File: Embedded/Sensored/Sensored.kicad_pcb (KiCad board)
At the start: 2 copper layers, 9 x 9.5 mm, 13 parts, among them U1 ICM-20948, U3 BME280

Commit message: Added Castellated Pins & Removed Micro SD Card
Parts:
- removed C10: 22uF, Capacitor_SMD:C_0603_1608Metric_Pad1.08x0.95mm_HandSolder
- removed C12: 0.1uF, Capacitor_SMD:C_0402_1005Metric
- added J1: Casselation, Simple_Connector:1mm_4P, F.Cu at (146.0, 109.5)
- added R1: 10K, Resistor_SMD:R_0402_1005Metric, F.Cu at (143.7, 105.5)
- added R2: 10K, Resistor_SMD:R_0402_1005Metric, F.Cu at (143.7, 104.6)
- moved C9 0.94 mm to (140.2, 111.3)
- moved C3 0.84 mm to (144.5, 111.2)
- moved C4 0.72 mm to (142.7, 111.3)
- moved U4 0.70 mm to (140.1, 109.9)
- moved C11 0.63 mm to (139.8, 108.5)
- moved C13 0.39 mm to (139.8, 107.3)
- moved C1 0.37 mm to (143.7, 106.5)
- moved C6 0.23 mm to (138.7, 105.9)
- moved C8 0.19 mm to (142.4, 106.0)
- moved U3 0.13 mm to (140.5, 105.5)
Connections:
- C9 pad 1: Vin -> +3V3
- U4 pad 3: Vin -> +3V3
- U4 pad 4: Vin -> +3V3
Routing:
- added copper zone on F.Cu, net +3V3
- added copper zone on B.Cu, net GND
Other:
- board size 9 x 9.5 mm -> 8 x 7.9 mm

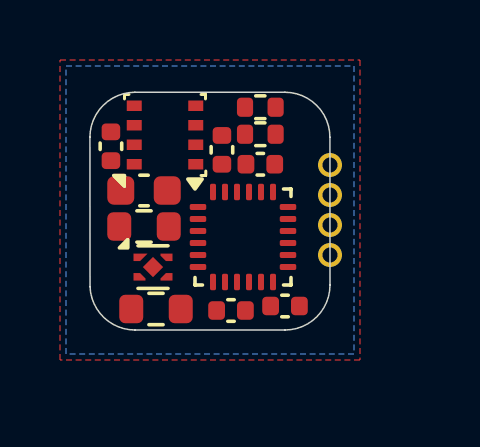
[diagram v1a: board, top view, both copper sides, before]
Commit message: Added Stabiliser GND Pins & Finished Routing
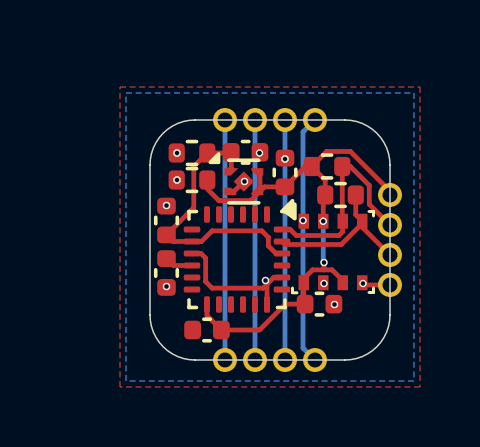
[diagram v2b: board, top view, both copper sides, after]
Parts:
- added J2: Casselation, Simple_Connector:1mm_4P, F.Cu at (142.5, 105.0)
- added J3: Casselation, Simple_Connector:1mm_4P, F.Cu at (142.5, 113.0)
- C11, C9: footprint Resistor_SMD:R_0603_1608Metric -> Resistor_SMD:R_0402_1005Metric
- C13: footprint Capacitor_SMD:C_0603_1608Metric -> Capacitor_SMD:C_0402_1005Metric
- moved U3 6.82 mm to (146.1, 109.4), turned to 0 degrees
- moved C8 6.08 mm to (145.7, 111.1), turned to 0 degrees
- moved C6 5.87 mm to (144.5, 106.8), turned to -90 degrees
- moved C9 4.46 mm to (141.4, 107.0)
- moved U4 4.16 mm to (143.1, 107.1)
- moved C1 3.65 mm to (140.6, 108.3), turned to -90 degrees
- moved C13 3.62 mm to (143.2, 106.1), turned to 0 degrees
- moved R1 3.35 mm to (146.3, 107.5)
- moved R2 2.97 mm to (145.9, 106.5)
- moved C11 2.93 mm to (141.4, 106.1)
- moved J1 2.83 mm to (148.0, 107.5), turned to 0 degrees
- moved C3 2.72 mm to (141.9, 112.0)
- moved C4 2.49 mm to (140.5, 110.1), turned to -90 degrees
- moved U1 0.78 mm to (142.9, 109.6), turned to -90 degrees
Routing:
- net GND: track 0.00 -> 39.1 mm, vias 0 -> 12
- net +3V3: track 0.00 -> 18.7 mm, vias 0 -> 2
- net +1V8: track 0.00 -> 9.37 mm
- net SDA: track 0.00 -> 7.11 mm
- net SCL: track 0.00 -> 5.66 mm
- net Net-(U1-REGOUT): track 0.00 -> 0.95 mm
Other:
- board size 8 x 7.9 mm -> 8 x 8 mm

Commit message: Added Markings & Component Adjustment
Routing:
- net GND: vias 12 -> 13
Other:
- board text added: "3V3 SDA SCL GND"

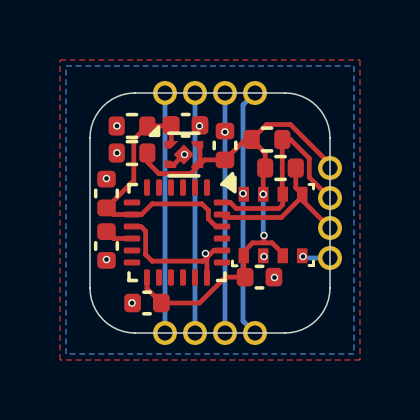
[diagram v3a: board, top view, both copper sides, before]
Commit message: Replaced Side GND Pins with GND EPad
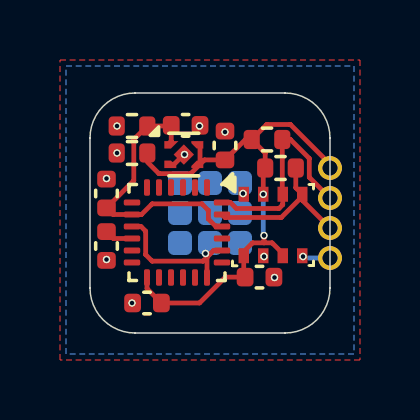
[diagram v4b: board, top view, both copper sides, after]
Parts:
- removed J3: Casselation, Simple_Connector:1mm_4P
- J2: value Casselation -> EPad; footprint Simple_Connector:1mm_4P -> Simple_Connector:1mm 3x3 Pad; moved to B.Cu
- moved J2 4.27 mm to (144.0, 109.0)
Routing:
- net GND: track 39.1 -> 6.80 mm

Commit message: Generated BOM, JLCPCB Assembly Parts, Production Files, Drill Positions
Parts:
- U4: value ~ -> TLV74018PDQNR
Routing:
- net (no net): vias 0 -> 4
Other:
- board size 8 x 8 mm -> 15 x 15 mm
- board text added: "Sensored"
- board text added: "V1.0"

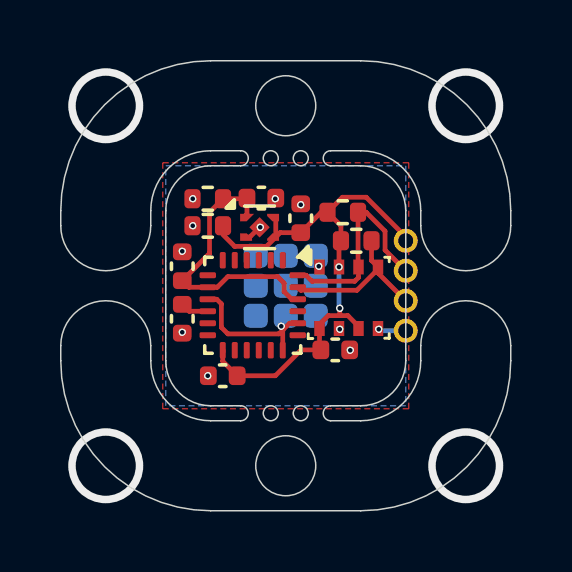
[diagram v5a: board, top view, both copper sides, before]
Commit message: Optimised JLCPCB Specific Parts
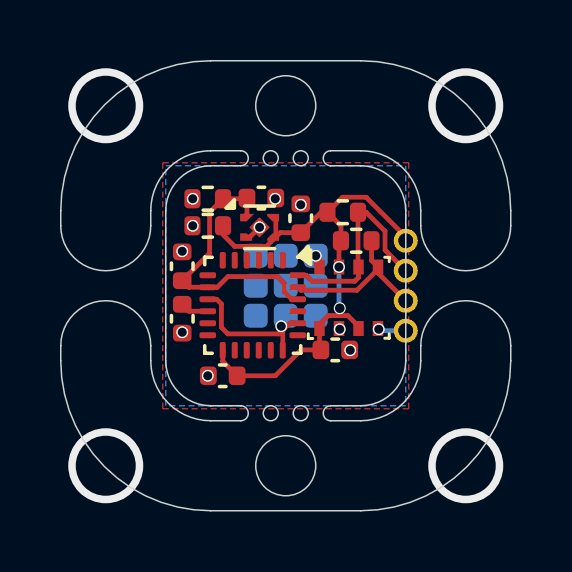
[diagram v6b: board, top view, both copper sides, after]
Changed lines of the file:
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@@
-	)
-	(segment
-		(start 145.124999 108.375)
-		(end 145.124999 108.374999)
-		(width 0.16)
-		(layer "F.Cu")
-		(net 1)
 	)
 	(segment
@@
 	)
 	(segment
-		(start 143.1275 107.0525)
-		(end 143.1475 107.0525)
-		(width 0.16)
-		(layer "F.Cu")
-		(net 1)
-	)
-	(segment
 		(start 141.42 112)
 		(end 141.4 112)
@@
 	)
 	(segment
+		(start 145.124999 108.124999)
+		(end 145.124999 108.375)
+		(width 0.16)
+		(layer "F.Cu")
+		(net 1)
+	)
+	(segment
 		(start 143.9 110.4)
 		(end 143.85 110.35)
@@
 	)
 	(segment
-		(start 143.1475 107.0525)
-		(end 143.15 107.05)
-		(width 0.16)
-		(layer "F.Cu")
-		(net 1)
-	)
-	(segment
 		(start 141.4 109.449999)
 		(end 141.699999 109.449999)
@@
 	)
 	(segment
+		(start 145 108)
+		(end 145.124999 108.124999)
+		(width 0.16)
+		(layer "F.Cu")
+		(net 1)
+	)
+	(segment
 		(start 140.89 107)
 		(end 140.9 107)
@@
 	)
 	(segment
-		(start 145.124999 108.374999)
-		(end 145.1 108.35)
-		(width 0.16)
-		(layer "F.Cu")
-		(net 1)
-	)
-	(segment
 		(start 142.5875 107.3775)
 		(end 142.8025 107.3775)
@@
 	)
 	(via
-		(at 143.15 107.05)
-		(size 0.25)
-		(drill 0.15)
+		(at 143.1275 107.0525)
+		(size 0.4)
+		(drill 0.3)
 		(layers "F.Cu" "B.Cu")
 		(net 1)
@@
 	(via
 		(at 140.9 106.1)
-		(size 0.25)
-		(drill 0.15)
+		(size 0.4)
+		(drill 0.3)
 		(layers "F.Cu" "B.Cu")
 		(net 1)
@@
 	(via
 		(at 140.55 107.85)
-		(size 0.25)
-		(drill 0.15)
+		(size 0.4)
+		(drill 0.3)
 		(layers "F.Cu" "B.Cu")
 		(net 1)
@@
 	(via
 		(at 140.9 107)
-		(size 0.25)
-		(drill 0.15)
+		(size 0.4)
+		(drill 0.3)
 		(layers "F.Cu" "B.Cu")
 		(net 1)
@@
 	(via
 		(at 146.15 111.15)
-		(size 0.25)
-		(drill 0.15)
+		(size 0.4)
+		(drill 0.3)
 		(layers "F.Cu" "B.Cu")
 		(net 1)
@@
 	(via
 		(at 141.4 112)
-		(size 0.25)
-		(drill 0.15)
+		(size 0.4)
+		(drill 0.3)
 		(layers "F.Cu" "B.Cu")
 		(net 1)
@@
 	(via
 		(at 143.85 110.35)
-		(size 0.25)
-		(drill 0.15)
-		(layers "F.Cu" "B.Cu")
-		(net 1)
-	)
-	(via
-		(at 145.1 108.35)
-		(size 0.25)
-		(drill 0.15)
+		(size 0.4)
+		(drill 0.3)
+		(layers "F.Cu" "B.Cu")
+		(net 1)
+	)
+	(via
+		(at 145 108)
+		(size 0.4)
+		(drill 0.3)
 		(layers "F.Cu" "B.Cu")
 		(net 1)
@@
 	(via
 		(at 145.8 110.45)
-		(size 0.25)
-		(drill 0.15)
+		(size 0.4)
+		(drill 0.3)
 		(layers "F.Cu" "B.Cu")
 		(net 1)
@@
 	(via
 		(at 147.1 110.45)
-		(size 0.25)
-		(drill 0.15)
+		(size 0.4)
+		(drill 0.3)
 		(layers "F.Cu" "B.Cu")
 		(net 1)
@@
 	(via
 		(at 144.5 106.3)
-		(size 0.25)
-		(drill 0.15)
+		(size 0.4)
+		(drill 0.3)
 		(layers "F.Cu" "B.Cu")
 		(net 1)
@@
 	(via
 		(at 140.55 110.55)
-		(size 0.25)
-		(drill 0.15)
+		(size 0.4)
+		(drill 0.3)
 		(layers "F.Cu" "B.Cu")
 		(net 1)
@@
 	(via
 		(at 143.65 106.1)
-		(size 0.25)
-		(drill 0.15)
+		(size 0.4)
+		(drill 0.3)
 		(layers "F.Cu" "B.Cu")
 		(net 1)
@@
 	(via
 		(at 145.8 109.75)
-		(size 0.25)
-		(drill 0.15)
+		(size 0.4)
+		(drill 0.32)
 		(layers "F.Cu" "B.Cu")
 		(net 3)
@@
 	(via
 		(at 145.775 108.375)
-		(size 0.25)
-		(drill 0.15)
-		(layers "F.Cu" "B.Cu")
-		(net 3)
+		(size 0.4)
+		(drill 0.3)
+		(layers "F.Cu" "B.Cu")
+		(net 3)

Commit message: Removed Obsolete Files
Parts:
- C6, C8: value 100nF -> 0.1uF
- U4: value TLV74018PDQNR -> TLV74318PDQNR3
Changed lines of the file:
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@@
 			)
 		)
-		(property "LCSC" ""
+		(property "LCSC" "C52923"
 			(at 0 0 180)
 			(unlocked yes)
@@
 			)
 		)
-		(property "LCSC" ""
+		(property "LCSC" "C1525"
 			(at 0 0 -90)
 			(unlocked yes)
@@
 			)
 		)
-		(property "LCSC" ""
+		(property "LCSC" "C92489"
 			(at 0 0 0)
 			(unlocked yes)
@@
 			)
 		)
-		(property "LCSC" ""
+		(property "LCSC" "C1525"
 			(at 0 0 180)
 			(unlocked yes)
@@
 			)
 		)
-		(property "LCSC" ""
+		(property "LCSC" "C25744"
 			(at 0 0 0)
 			(unlocked yes)
@@
 			)
 		)
-		(property "LCSC" ""
+		(property "LCSC" "C1525"
 			(at 0 0 -90)
 			(unlocked yes)
@@
 			)
 		)
-		(property "Value" "100nF"
+		(property "Value" "0.1uF"
 			(at 0 1.16 90)
 			(layer "F.Fab")
@@
 			)
 		)
-		(property "LCSC" ""
+		(property "LCSC" "C1525"
 			(at 0 0 -90)
 			(unlocked yes)
@@
 			)
 		)
-		(property "Value" "100nF"
+		(property "Value" "0.1uF"
 			(at 0 1.16 0)
 			(layer "F.Fab")
@@
 			)
 		)
-		(property "LCSC" ""
+		(property "LCSC" "C1525"
 			(at 0 0 0)
 			(unlocked yes)
@@
 			)
 		)
-		(property "LCSC" ""
+		(property "LCSC" "C15525"
 			(at 0 0 0)
 			(unlocked yes)
@@
 			)
 		)
-		(property "LCSC" ""
+		(property "LCSC" "C25744"
 			(at 0 0 0)
 			(unlocked yes)
@@
 			)
 		)
-		(property "Value" "TLV74018PDQNR"
+		(property "Value" "TLV74318PDQNR3"
 			(at 0 1.5 0)
 			(layer "F.Fab")
@@
 			)
 		)
-		(property "LCSC" ""
+		(property "LCSC PN" "C2860843"
 			(at 0 0 0)
 			(unlocked yes)
@@
 			)
 		)
-		(property "LCSC" ""
+		(property "LCSC" "C52923"
 			(at 0 0 180)
 			(unlocked yes)
@@
 			)
 		)
-		(property "LCSC" ""
+		(property "LCSC PN" "C726001"
 			(at 0 0 -90)
 			(unlocked yes)

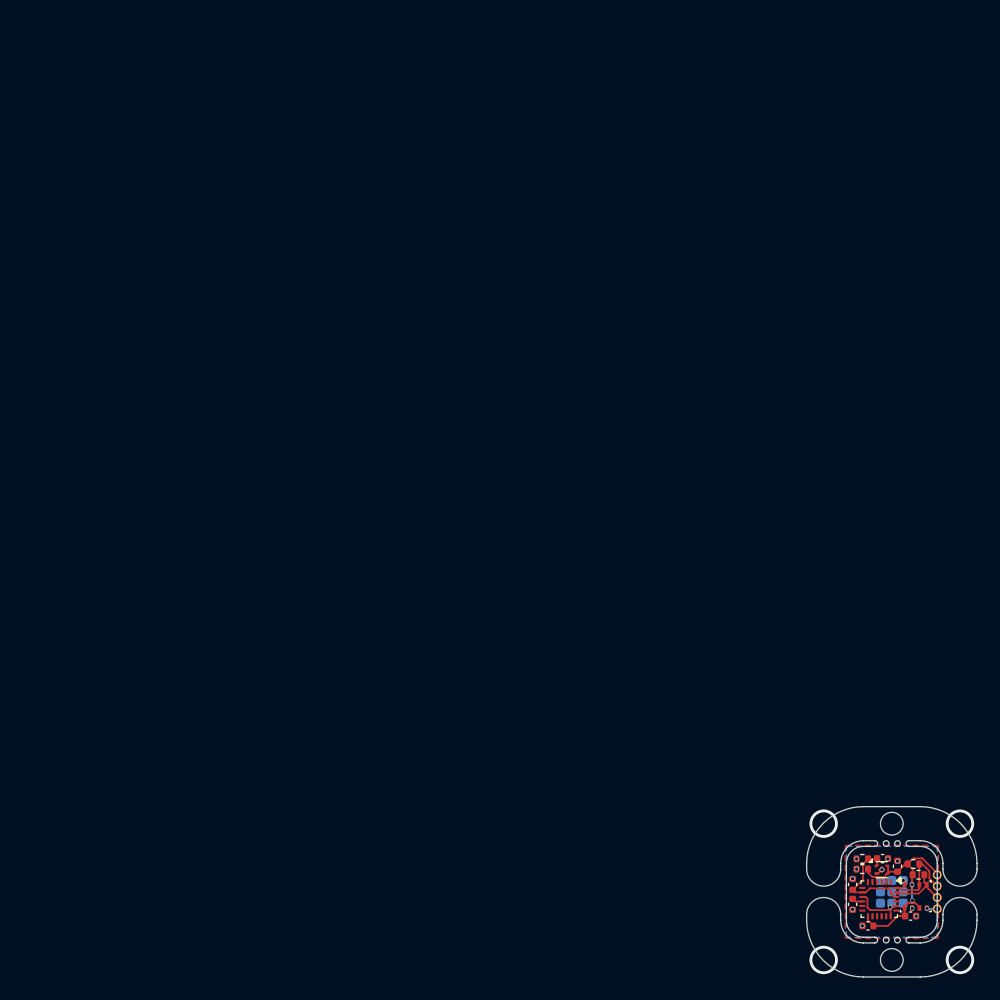
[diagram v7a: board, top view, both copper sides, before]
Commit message: Modified Outline & Component Placements for V2
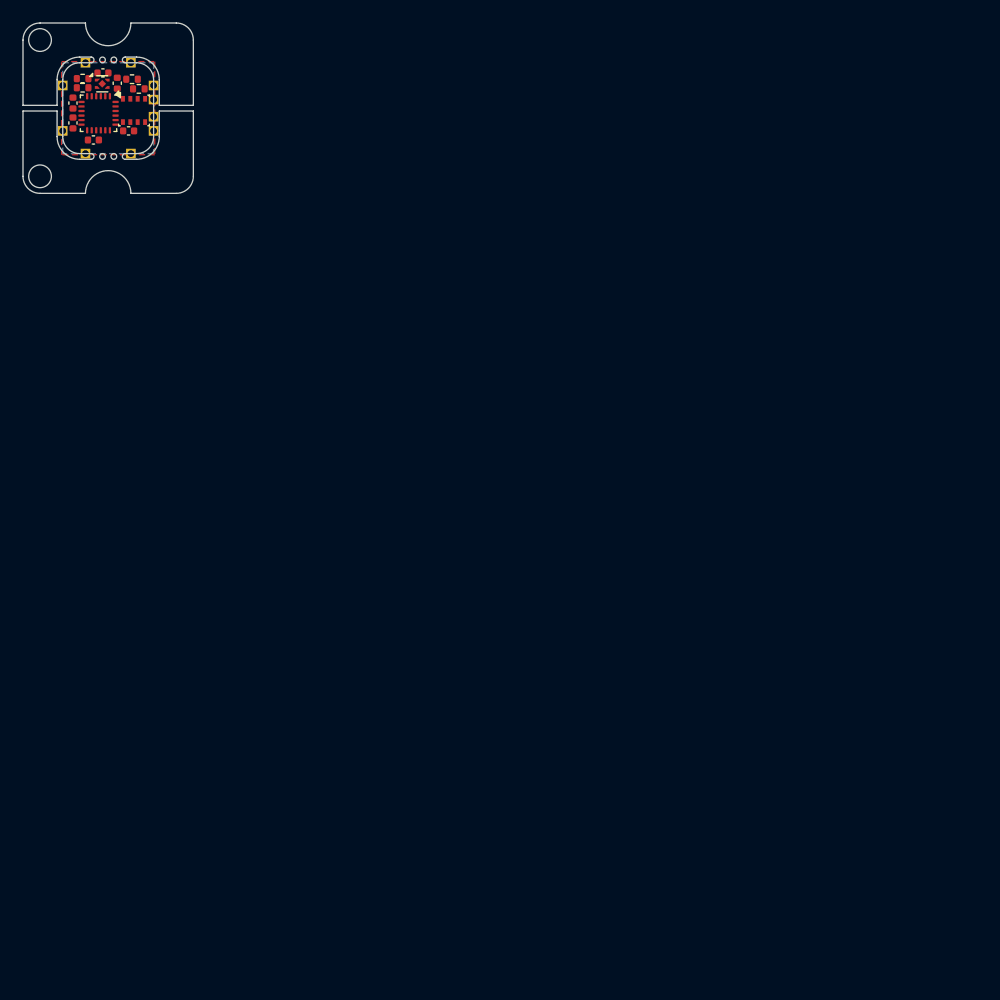
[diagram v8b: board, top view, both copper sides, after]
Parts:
- added J10: SCL, Custom Connectors:1mm Pads, B.Cu at (79.0, 40.8)
- added J3: GND, Custom Connectors:1mm Pads, B.Cu at (79.0, 42.0)
- added J4: PWR, Custom Connectors:1mm Pads, B.Cu at (73.0, 36.0)
- added J5: GND, Custom Connectors:1mm Pads, B.Cu at (77.0, 36.0)
- added J6: PWR, Custom Connectors:1mm Pads, B.Cu at (71.0, 42.0)
- added J7: GND, Custom Connectors:1mm Pads, B.Cu at (71.0, 38.0)
- added J8: PWR, Custom Connectors:1mm Pads, B.Cu at (77.0, 44.0)
- added J9: GND, Custom Connectors:1mm Pads, B.Cu at (73.0, 44.0)
- J1: value Casselation -> SDA; footprint Simple_Connector:1mm_4P -> Custom Connectors:1mm Pads; moved to B.Cu
- J2: value EPad -> PWR; footprint Simple_Connector:1mm 3x3 Pad -> Custom Connectors:1mm Pads
- moved U3 97.6 mm to (77.3, 40.2)
- moved C8 97.6 mm to (76.8, 42.0)
- moved U1 97.5 mm to (74.2, 40.5)
- moved R2 97.5 mm to (77.1, 37.5)
- moved R1 97.5 mm to (77.7, 38.3)
- moved U4 97.5 mm to (74.5, 37.9)
- moved C13 97.5 mm to (74.5, 36.9)
- moved C6 97.3 mm to (75.8, 37.8)
- moved C1 97.2 mm to (71.9, 39.5)
- moved C4 97.2 mm to (71.9, 41.3)
- moved C9 97.2 mm to (72.8, 38.2)
- moved C3 97.2 mm to (73.7, 42.8), turned to 0 degrees
- moved C11 97.1 mm to (72.8, 37.4)
- moved J1 97.1 mm to (79.0, 39.2), turned to 180 degrees
- moved J2 96.3 mm to (79.0, 38.0), turned to 180 degrees
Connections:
- J1 pad 1: +3V3 -> SDA
- J2 pad 1: GND -> +3V3
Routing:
- net +3V3: track 18.7 -> 0.00 mm, vias 2 -> 0
- net +1V8: track 9.37 -> 0.00 mm
- net GND: track 7.17 -> 0.00 mm, vias 13 -> 0
- net SDA: track 7.11 -> 0.00 mm
- net SCL: track 5.66 -> 0.00 mm
- net Net-(U1-REGOUT): track 0.95 -> 0.00 mm
- net (no net): vias 4 -> 0
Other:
- outline, holes or cut-outs redrawn
- board text added: "V2.0"
- board text removed: "3V3 SDA SCL GND"
- board text removed: "V1.0"
